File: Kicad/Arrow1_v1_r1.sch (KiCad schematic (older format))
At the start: 3 parts

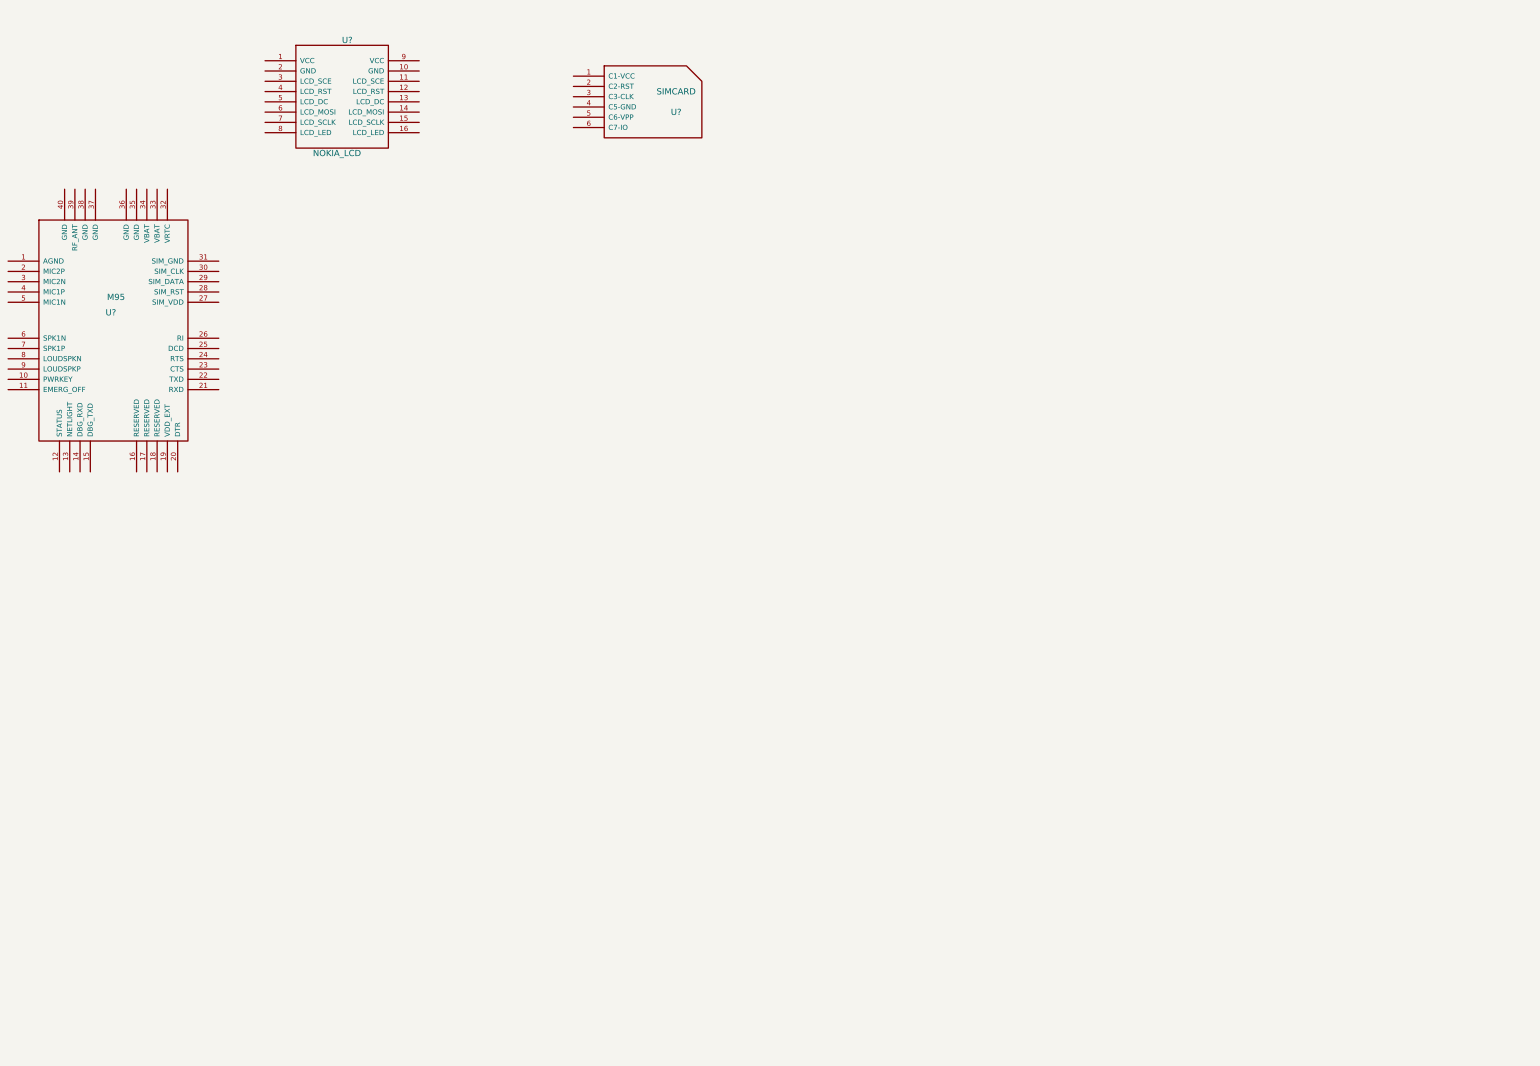
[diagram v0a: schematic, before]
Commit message: kicad advance
m95 schematic components almost done (only antenna missing)
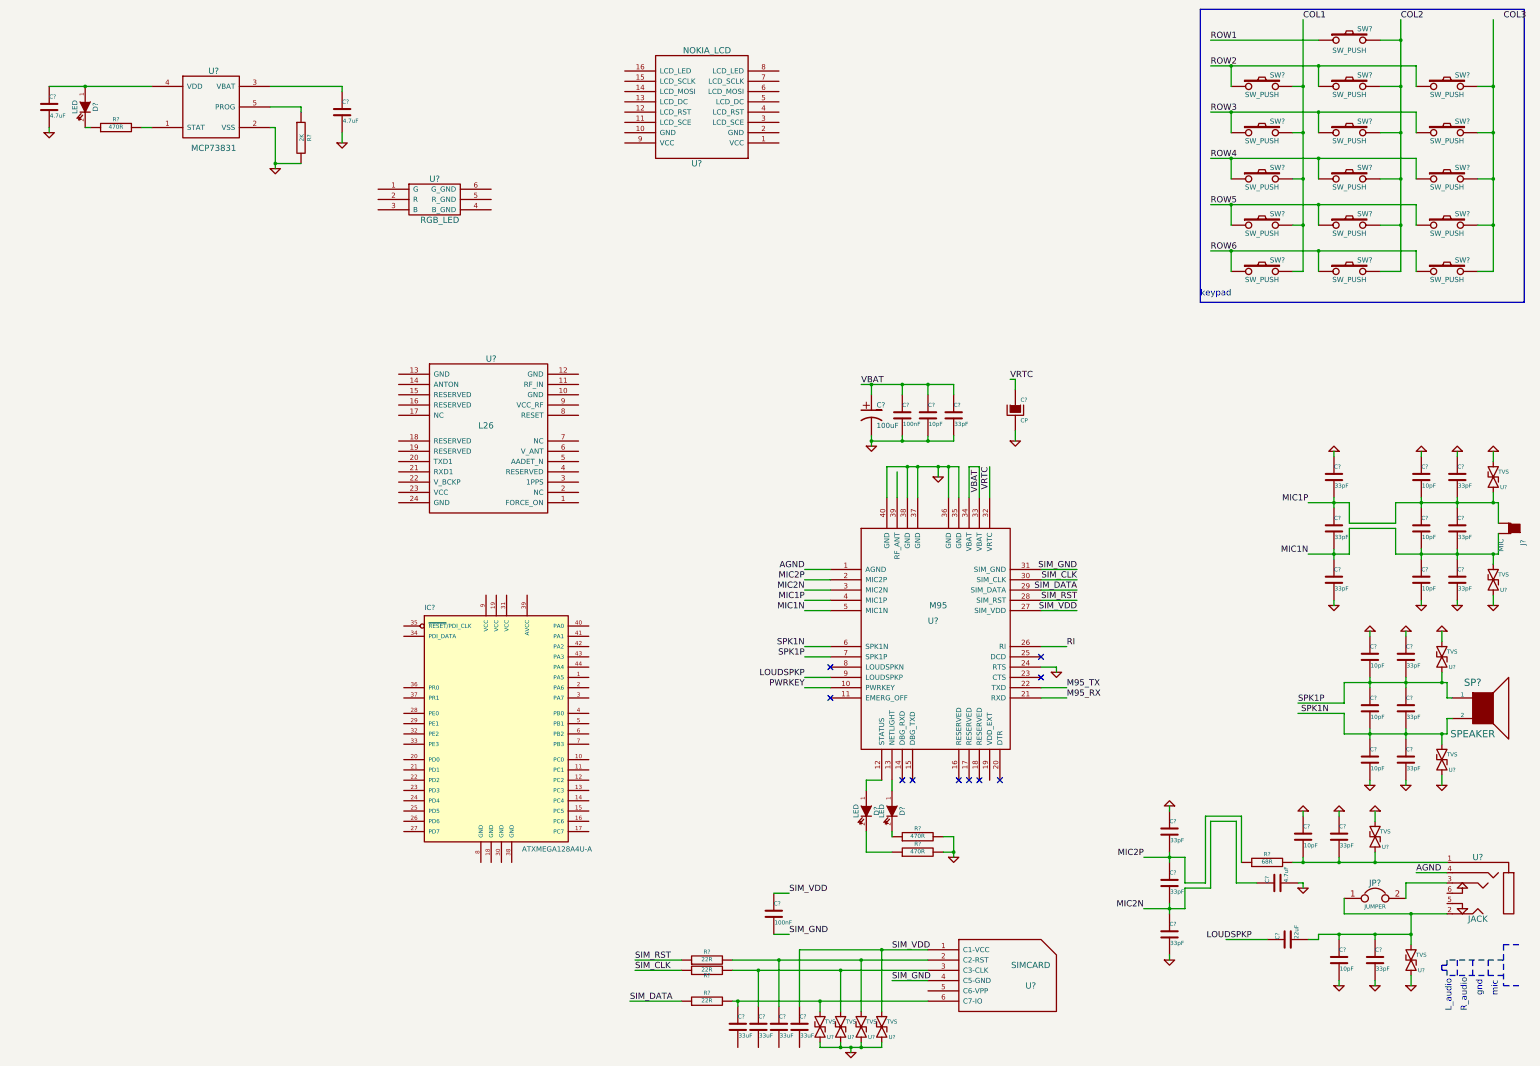
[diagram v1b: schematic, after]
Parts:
- added C? (x3): 4.7uF, ~, symbol C
- added C? (x2): 100nF, ~, symbol C
- added C? (x9): 10pF, ~, symbol C
- added C? (x15): 33pF, ~, symbol C
- added C?: 100uF, ~, symbol CP1
- added C?: CP, ~, symbol CP
- added C?: 22uF, ~, symbol C
- added C? (x4): 33uF, ~, symbol C
- added D? (x3): LED, ~, symbol LED
- added IC?: ATXMEGA128A4U-A, TQFP44, symbol ATXMEGA128A4U-A
- added J?: MIC, ~, symbol TEMPLATE
- added JP?: JUMPER, ~, symbol JUMPER
- added R?: 2K, ~, symbol R
- added R? (x3): 470R, ~, symbol R
- added R?: 68R, ~, symbol R
- added R? (x3): 22R, ~, symbol R
- added SP?: SPEAKER, ~, symbol SPEAKER
- added SW? (x16): SW_PUSH, ~, symbol SW_PUSH
- added U?: MCP73831, symbol MCP73831
- added U?: RGB_LED, symbol RGB_LED
- added U?: L26, symbol L26
- added U? (x10): TVS, symbol TVS
- added U?: JACK, symbol JACK
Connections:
- net SIM_VDD: now reaches U?.1 (C1-VCC)
- net SIM_VDD: now also U?.27 (SIM_VDD), C?.1, C?.1, U?.~
- net at U?.2 (C2-RST): now also C?.1, R?.2, U?.~
- net at U?.3 (C3-CLK): now also C?.1, R?.2, U?.~
- net SIM_GND: now reaches U?.4 (C5-GND)
- net SIM_GND: now also U?.31 (SIM_GND), C?.2
- net at U?.6 (C7-IO): now also C?.1, R?.2, U?.~
- net AGND: now reaches U?.1 (AGND)
- net AGND: now also U?.4
- net PWRKEY: now reaches U?.10 (PWRKEY)
- net at U?.12 (STATUS): now also D?.1 (A)
- net at U?.13 (NETLIGHT): now also D?.1 (A)
- net MIC2P: now reaches U?.2 (MIC2P)
- net MIC2P: now also C?.1, C?.2, R?.1
- net M95_RX: now reaches U?.21 (RXD)
- net M95_TX: now reaches U?.22 (TXD)
- net GND: now reaches U?.24 (RTS)
- net GND: now also U?.35 (GND), U?.36 (GND), U?.37 (GND), U?.38 (GND), U?.40 (GND), C?.1, C?.1, C?.1, C?.1, C?.1, C?.1, C?.1, C?.1, C?.2, C?.2, C?.2, C?.2, C?.2, C?.2, C?.2, C?.2, C?.2, C?.2, C?.2, C?.2, C?.2, C?.2, C?.2, C?.2, R?.2, R?.2, R?.2, U?.2 (VSS), U?.~, U?.~, U?.~, U?.~, U?.~, U?.~, U?.~, U?.~, U?.~, U?.~
- net RI: now reaches U?.26 (RI)
- net SIM_RST: now reaches U?.28 (SIM_RST)
- net SIM_RST: now also R?.1
- net SIM_DATA: now reaches U?.29 (SIM_DATA)
- net SIM_DATA: now also R?.1
- net MIC2N: now reaches U?.3 (MIC2N)
- net MIC2N: now also C?.1, C?.1, C?.2
- net SIM_CLK: now reaches U?.30 (SIM_CLK)
- net SIM_CLK: now also R?.1
- net VRTC: now reaches U?.32 (VRTC)
- net VRTC: now also C?.1
- net VBAT: now reaches U?.33 (VBAT)
- net VBAT: now also U?.34 (VBAT), C?.1, C?.1, C?.1, C?.1
- net MIC1P: now reaches U?.4 (MIC1P)
- net MIC1P: now also C?.1, C?.1, C?.1, C?.2, C?.2, C?.2, J?.1, U?.~
- net MIC1N: now reaches U?.5 (MIC1N)
- net MIC1N: now also C?.1, C?.1, C?.1, C?.2, C?.2, C?.2, J?.2, U?.~
- net SPK1N: now reaches U?.6 (SPK1N)
- net SPK1N: now also C?.1, C?.1, C?.2, C?.2, SP?.2, U?.~
- net SPK1P: now reaches U?.7 (SPK1P)
- net SPK1P: now also C?.1, C?.1, C?.2, C?.2, SP?.1, U?.~
- net LOUDSPKP: now reaches U?.9 (LOUDSPKP)
- net LOUDSPKP: now also C?.1
- new net: R?.2, U?.1 (STAT)
- new net: C?.1, U?.3 (VBAT)
- new net: C?.1, D?.1 (A), U?.4 (VDD)
- new net: R?.1, U?.5 (PROG)
- new net: D?.2 (K), R?.1 (x3)
- new net: SW?.2, SW?.2, SW?.2, SW?.2, SW?.2
- new net: C?.2, C?.2, R?.2, U?.1, U?.~
- new net: C?.1, C?.1, C?.2, JP?.1, U?.2, U?.~
- new net: JP?.2, U?.3
- new net COL1: SW?.2, SW?.2, SW?.2, SW?.2, SW?.2
- new net COL2: SW?.2, SW?.2, SW?.2, SW?.2, SW?.2, SW?.2
- new net ROW1: SW?.1
- new net ROW2: SW?.1, SW?.1, SW?.1
- new net ROW3: SW?.1, SW?.1, SW?.1
- new net ROW4: SW?.1, SW?.1, SW?.1
- new net ROW5: SW?.1, SW?.1, SW?.1
- new net ROW6: SW?.1, SW?.1, SW?.1
- no-connect marks 0 -> 10
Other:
- note added: "L_audio"
- note added: "R_audio"
- note added: "gnd\n"
- note added: "keypad"
- note added: "mic\n"
- moved on the sheet: U?

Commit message: update
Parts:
- added C? (x4): NM, ~, symbol C
- added C? (x2): 4.7uF, ~, symbol C
- added C? (x2): 100nF, ~, symbol C
- added C? (x2): 1000uF, ~, symbol CP1
- added C? (x2): 0.1uF, ~, symbol C
- added C?: CP, ~, symbol CP
- added D?: RB520S30T1G, ~, symbol DIODE
- added D?: LED, ~, symbol LED
- added D?: DIODE, ~, symbol DIODE
- added P?: CONN_2, symbol CONN_2
- added Q? (x2): NPN, ~, symbol NPN
- added R? (x2): 0R, ~, symbol R
- added R?: 1K, ~, symbol R
- added R? (x4): 470R, ~, symbol R
- added R?: 10R, ~, symbol R
- added R? (x2): 4.7K, ~, symbol R
- added R?: 100R, ~, symbol R
- added R? (x4): 100K, ~, symbol R
- added SP?: BUZZER, ~, symbol SPEAKER
- added U? (x2): ANT, symbol ANT
- added U? (x2): SMA_CON, symbol SMA_CON
- added U?: SD_CONNECTOR, symbol SD_CONNECTOR
- added U? (x3): PREPOL_BJT, symbol PREPOL_BJT
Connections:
- net VBAT is gone; now on net VCC: C?.1, C?.1, C?.1, C?.1, U?.33 (VBAT), U?.34 (VBAT)
- net GND: now also U?.10 (GND), U?.12 (GND), U?.13 (GND), U?.2 (GND), U?.24 (GND), C?.2, C?.2, C?.2, C?.2, C?.2, C?.2, C?.2, C?.2, C?.2, C?.2, C?.2, C?.2, C?.2, P?.1 (P1), Q?.1 (E), R?.2, U?.6 (VSS), U?.G1 (GND), U?.G2 (GND), U?.G3 (GND), U?.G4 (POL), U?.~, U?.~, U?.~, U?.~, U?.~
- net VCC: now reaches U?.1 (VCC)
- net VCC: now also C?.1, U?.23 (VCC), U?.3 (VBAT), C?.1, C?.1, C?.1, C?.1, C?.1, C?.1, D?.1 (A), D?.2 (K), P?.2 (PM), R?.1, R?.1, R?.1, R?.1, R?.1, R?.1, R?.1, R?.2, SP?.1, U?.4 (VDD)
- net LCD_SCE: now reaches U?.3 (LCD_SCE)
- net LCD_RST: now reaches U?.4 (LCD_RST)
- net LCD_DC: now reaches U?.5 (LCD_DC)
- net LCD_MOSI: now reaches U?.6 (LCD_MOSI)
- net LCD_SCLK: now reaches U?.7 (LCD_SCLK)
- net at U?.8 (LCD_LED): now also Q?.1 (E)
- net M95_ANT: now reaches U?.39 (RF_ANT)
- net M95_ANT: now also C?.1, R?.1
- net at U?.1 (G): now also R?.2
- net at U?.2 (R): now also R?.2
- net at U?.3 (B): now also R?.2
- net at U?.4 (B_GND): now also U?.~
- net at U?.5 (R_GND): now also U?.~
- net at U?.6 (G_GND): now also U?.~
- net L26_FORCE_ON: now reaches U?.1 (FORCE_ON)
- net L26_ANT: now reaches U?.11 (RF_IN)
- net L26_ANT: now also C?.1, R?.1
- net L26_TX: now reaches U?.20 (TXD1)
- net L26_RX: now reaches U?.21 (RXD1)
- net V_BCKP: now reaches U?.22 (V_BCKP)
- net V_BCKP: now also C?.1, C?.1, C?.1, R?.1
- net at U?.3 (1PPS): now also D?.1 (A)
- net at U?.6 (V_ANT): now also R?.2
- net L26_RST: now reaches U?.8 (RESET)
- net at U?.9 (VCC_RF): now also R?.1
- new net: C?.1, R?.2, U?.~, U?.~ (x2)
- new net: D?.2 (K), R?.2
- new net: D?.2 (K), R?.1
- new net: D?.1 (A), Q?.3 (C), SP?.2
- new net: Q?.2 (B), R?.2 (x2)
- new net: Q?.3 (C), R?.1
- new net BUZZ: R?.1
- new net B_PWM: U?.~
- new net CD: U?.G5 (DET)
- new net G_PWM: U?.~
- new net LCD_LED: R?.1
- new net R_PWM: U?.~
- new net SD_CS: R?.2, U?.2 (CD/DAT3)
- new net SD_MISO: R?.2, U?.7 (DAT0)
- new net SD_MOSI: R?.2, U?.3 (CMD)
- new net SD_SCK: R?.2, U?.5 (CLK)
- no-connect marks 10 -> 23
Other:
- moved on the sheet: C?, D?, IC?, J?, JP?, R?, SP?, U?
